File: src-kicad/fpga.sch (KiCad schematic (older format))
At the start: 4 parts, among them U1 iCE40HX1K-TQ144

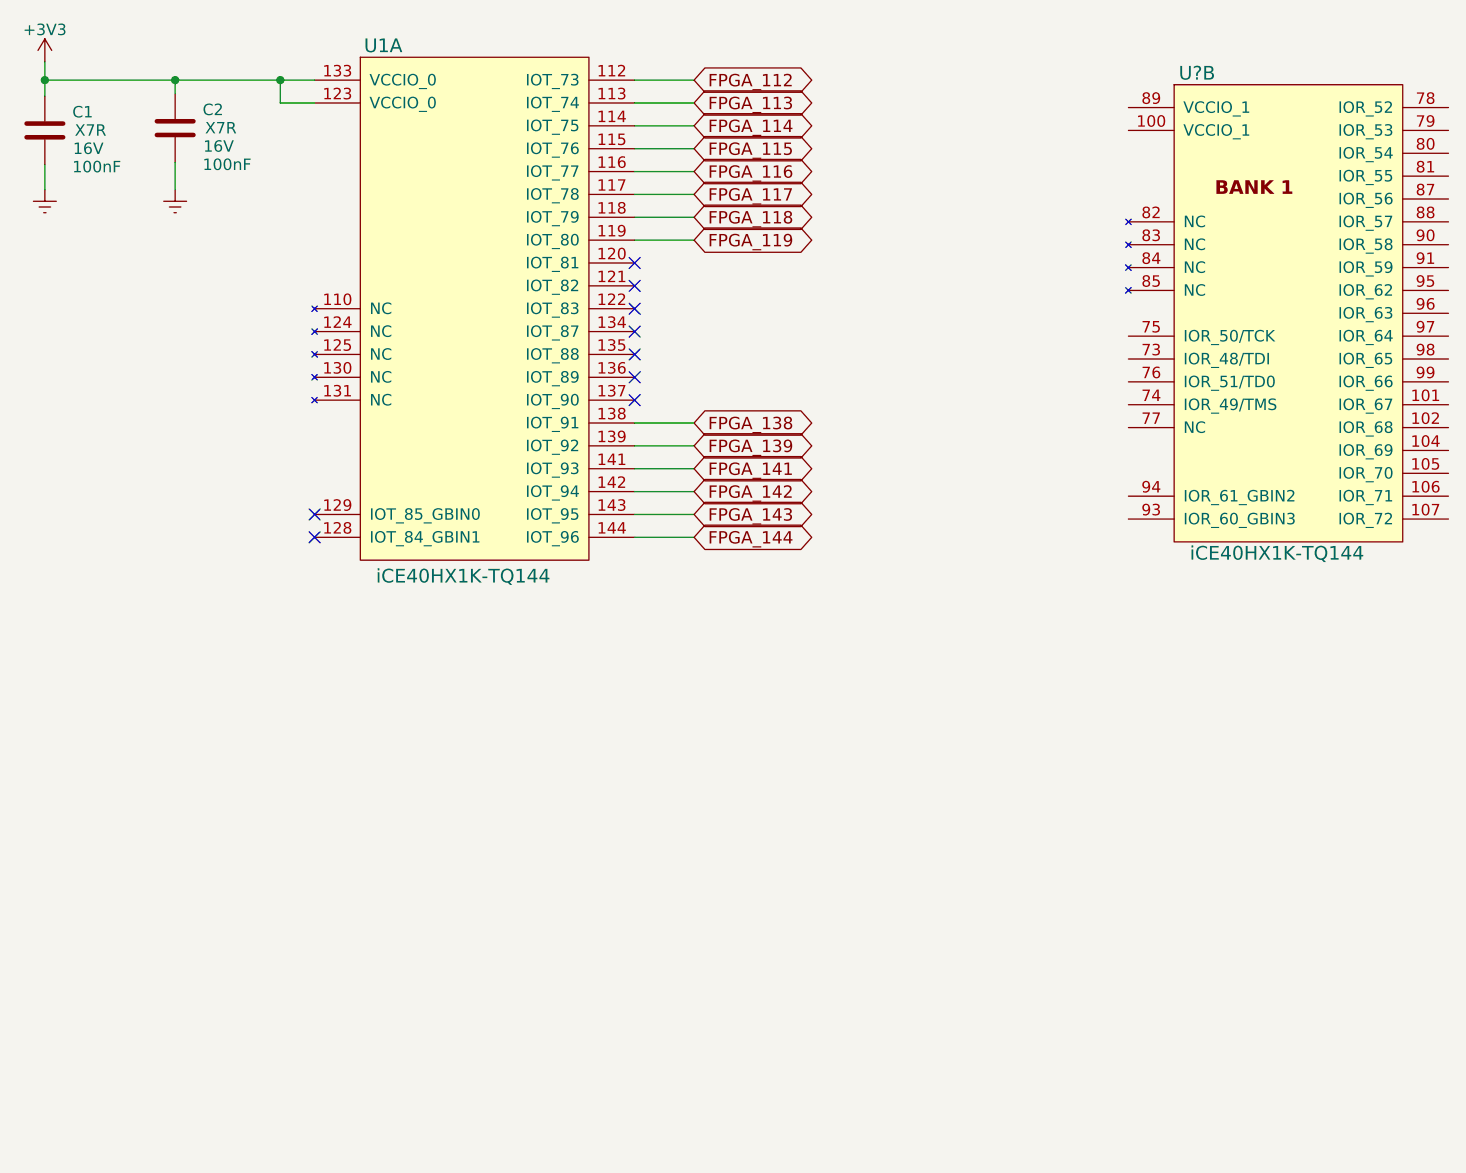
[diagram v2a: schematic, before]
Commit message: Kicad. FPGA: Bank 1 added to schematic
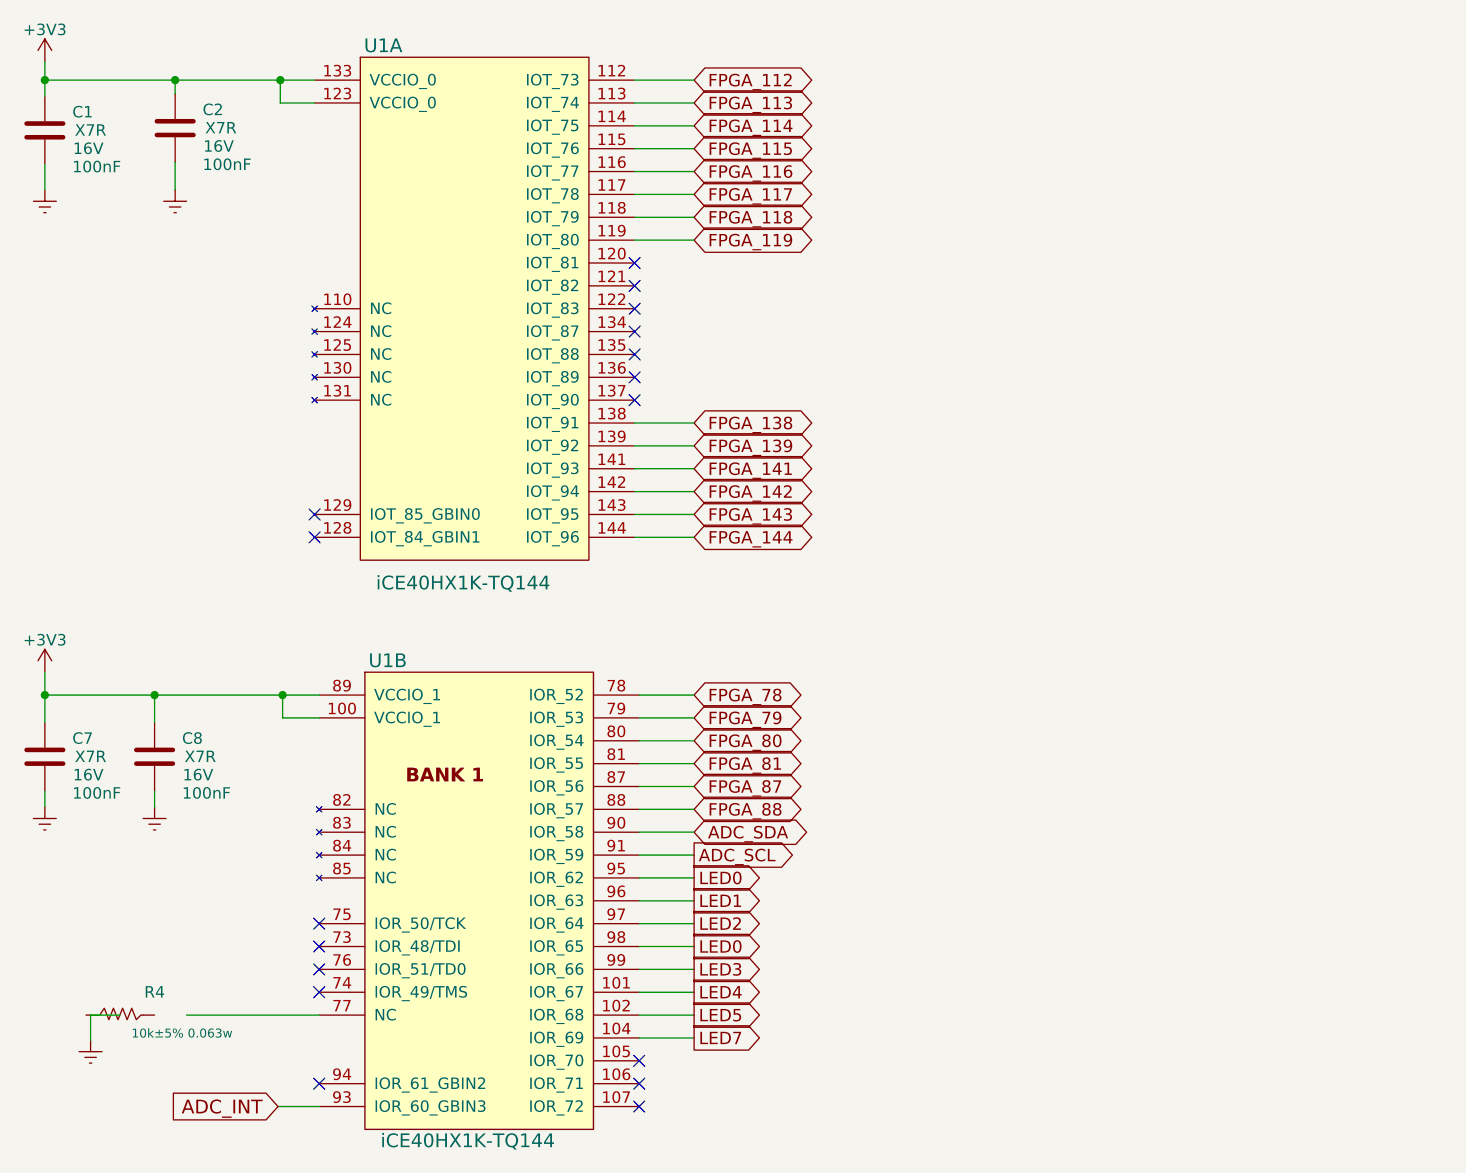
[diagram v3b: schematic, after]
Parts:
- added C7, C8: 100nF, symbol C
- added R4: 10k±5% 0.063w, symbol R
- gave numbers to parts that had none: 1
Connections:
- net labels added: ADC_INT, ADC_SCL, ADC_SDA, FPGA_78, FPGA_79, FPGA_80, FPGA_81, FPGA_87, FPGA_88, LED0, LED1, LED2, LED3, LED4, LED5, LED7
- wire segments 21 -> 48
- no-connect marks 9 -> 17
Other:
- moved on the sheet: U1B
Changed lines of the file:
@@
 EESchema Schematic File Version 2
-LIBS:power
-LIBS:device
 LIBS:transistors
 LIBS:conn
@@
 $EndDescr
 $Comp
-L iCE40HX1K-TQ144 U1
-U 1 1 5742DE36
-P 2140 1010
-F 0 "U1" H 2440 1160 60  0000 C CNN
-F 1 "iCE40HX1K-TQ144" H 2790 -1160 60  0000 C CNN
-F 2 "" H 2440 610 60  0000 C CNN
-F 3 "" H 2440 610 60  0000 C CNN
-	1    2140 1010
-	1    0    0    -1
-$EndComp
-$Comp
 L C C1
 U 1 1 5742E2A9
@@
 $EndComp
 $Comp
-L +3V3 #PWR?
+L +3V3 #PWR01
 U 1 1 5742EB21
 P 960 930
-F 0 "#PWR?" H 960 780 50  0001 C CNN
+F 0 "#PWR01" H 960 780 50  0001 C CNN
 F 1 "+3V3" H 960 1070 50  0000 C CNN
 F 2 "" H 960 930 50  0000 C CNN
@@
 	1    0    0    -1
 $EndComp
-Wire Wire Line
-	960  930  960  1080
-$Comp
-L GNDREF #PWR?
+$Comp
+L GNDREF #PWR02
 U 1 1 5742F120
 P 960 1490
-F 0 "#PWR?" H 960 1240 50  0001 C CNN
+F 0 "#PWR02" H 960 1240 50  0001 C CNN
 F 1 "GNDREF" H 960 1340 50  0001 C CNN
 F 2 "" H 960 1490 50  0000 C CNN
@@
 	1    0    0    -1
 $EndComp
-Wire Wire Line
-	960  1490 960  1380
 $Comp
 L C C2
@@
 $EndComp
 $Comp
-L GNDREF #PWR?
+L GNDREF #PWR03
 U 1 1 5742F317
 P 1530 1490
-F 0 "#PWR?" H 1530 1240 50  0001 C CNN
+F 0 "#PWR03" H 1530 1240 50  0001 C CNN
 F 1 "GNDREF" H 1530 1340 50  0001 C CNN
 F 2 "" H 1530 1490 50  0000 C CNN
@@
 	1    0    0    -1
 $EndComp
-Wire Wire Line
-	1530 1370 1530 1490
-Wire Wire Line
-	960  1010 2140 1010
-Connection ~ 960  1010
-Wire Wire Line
-	1530 1070 1530 1010
-Connection ~ 1530 1010
-Wire Wire Line
-	2140 1110 1990 1110
-Wire Wire Line
-	1990 1110 1990 1010
-Connection ~ 1990 1010
 NoConn ~ 2140 2910
 NoConn ~ 2140 3010
-Wire Wire Line
-	3540 1010 3800 1010
 Text GLabel 3800 1010 2    54   BiDi ~ 0
 FPGA_112
 Text GLabel 3800 1110 2    54   BiDi ~ 0
 FPGA_113
-Wire Wire Line
-	3540 1110 3800 1110
 Text GLabel 3800 1210 2    54   BiDi ~ 0
 FPGA_114
@@
 Text GLabel 3800 1710 2    54   BiDi ~ 0
 FPGA_119
-Wire Wire Line
-	3540 1210 3800 1210
-Wire Wire Line
-	3800 1310 3540 1310
-Wire Wire Line
-	3540 1410 3800 1410
-Wire Wire Line
-	3800 1510 3540 1510
-Wire Wire Line
-	3540 1610 3800 1610
-Wire Wire Line
-	3800 1710 3540 1710
 Text GLabel 3800 2510 2    54   BiDi ~ 0
 FPGA_138
@@
 Text GLabel 3800 3010 2    54   BiDi ~ 0
 FPGA_144
-Wire Wire Line
-	3540 3010 3800 3010
-Wire Wire Line
-	3800 2910 3540 2910
-Wire Wire Line
-	3540 2810 3800 2810
-Wire Wire Line
-	3800 2710 3540 2710
-Wire Wire Line
-	3540 2610 3800 2610
-Wire Wire Line
-	3540 2510 3800 2510
 NoConn ~ 3540 1810
 NoConn ~ 3540 1910
@@
 NoConn ~ 3540 2410
 $Comp
-L iCE40HX1K-TQ144 U?
+L iCE40HX1K-TQ144 U1
 U 2 1 57436BD0
-P 5700 1130
-F 0 "U?" H 6000 1280 60  0000 C CNN
-F 1 "iCE40HX1K-TQ144" H 6350 -820 60  0000 C CNN
-F 2 "" H 6000 730 60  0000 C CNN
-F 3 "" H 6000 730 60  0000 C CNN
-	2    5700 1130
-	1    0    0    -1
-$EndComp
+P 2160 3700
+F 0 "U1" H 2460 3850 60  0000 C CNN
+F 1 "iCE40HX1K-TQ144" H 2810 1750 60  0000 C CNN
+F 2 "" H 2460 3300 60  0000 C CNN
+F 3 "" H 2460 3300 60  0000 C CNN
+	2    2160 3700
+	1    0    0    -1
+$EndComp
+$Comp
+L C C7
+U 1 1 5743AB85
+P 960 3970
+F 0 "C7" H 1080 4050 50  0000 L CNN
+F 1 "100nF" H 1080 3810 50  0000 L CNN
+F 2 "" H 998 3820 50  0000 C CNN
+F 3 "" H 960 3970 50  0000 C CNN
+F 4 "X7R" H 1160 3970 50  0000 C CNN "class"
+F 5 "16V" H 1150 3890 50  0000 C CNN "Voltage"
+	1    960  3970
+	1    0    0    -1
+$EndComp
+$Comp
+L +3V3 #PWR04
+U 1 1 5743AD45
+P 960 3600
+F 0 "#PWR04" H 960 3450 50  0001 C CNN
+F 1 "+3V3" H 960 3740 50  0000 C CNN
+F 2 "" H 960 3600 50  0000 C CNN
+F 3 "" H 960 3600 50  0000 C CNN
+	1    960  3600
+	1    0    0    -1
+$EndComp
+$Comp
+L GNDREF #PWR05
+U 1 1 5743B1A8
+P 960 4190
+F 0 "#PWR05" H 960 3940 50  0001 C CNN
+F 1 "GNDREF" H 960 4040 50  0001 C CNN
+F 2 "" H 960 4190 50  0000 C CNN
+F 3 "" H 960 4190 50  0000 C CNN
+	1    960  4190
+	1    0    0    -1
+$EndComp
+$Comp
+L C C8
+U 1 1 5743B372
+P 1440 3970
+F 0 "C8" H 1560 4050 50  0000 L CNN
+F 1 "100nF" H 1560 3810 50  0000 L CNN
+F 2 "" H 1478 3820 50  0000 C CNN
+F 3 "" H 1440 3970 50  0000 C CNN
+F 4 "X7R" H 1640 3970 50  0000 C CNN "class"
+F 5 "16V" H 1630 3890 50  0000 C CNN "Voltage"
+	1    1440 3970
+	1    0    0    -1
+$EndComp
+$Comp
+L GNDREF #PWR06
+U 1 1 5743B3FC
+P 1440 4190
+F 0 "#PWR06" H 1440 3940 50  0001 C CNN
+F 1 "GNDREF" H 1440 4040 50  0001 C CNN
+F 2 "" H 1440 4190 50  0000 C CNN
+F 3 "" H 1440 4190 50  0000 C CNN
+	1    1440 4190
+	1    0    0    -1
+$EndComp
+$Comp
+L iCE40HX1K-TQ144 U1
+U 1 1 5743108E
+P 2140 1010
+F 0 "U1" H 2440 1160 60  0000 C CNN
+F 1 "iCE40HX1K-TQ144" H 2790 -1190 60  0000 C CNN
+F 2 "" H 2440 610 60  0000 C CNN
+F 3 "" H 2440 610 60  0000 C CNN
+	1    2140 1010
+	1    0    0    -1
+$EndComp
+$Comp
+L R R4
+U 1 1 574319A2
+P 1440 5100
+F 0 "R4" V 1340 5100 50  0000 C CNN
+F 1 "10k±5% 0.063w" V 1520 5220 39  0000 C CNN
+F 2 "" V 1370 5100 50  0000 C CNN
+F 3 "" H 1440 5100 50  0000 C CNN
+	1    1440 5100
+	0    1    1    0
+$EndComp
+$Comp
+L GNDREF #PWR07
+U 1 1 57431C0E
+P 1160 5210
+F 0 "#PWR07" H 1160 4960 50  0001 C CNN
+F 1 "GNDREF" H 1160 5060 50  0001 C CNN
+F 2 "" H 1160 5210 50  0000 C CNN
+F 3 "" H 1160 5210 50  0000 C CNN
+	1    1160 5210
+	1    0    0    -1
+$EndComp
+Wire Wire Line
+	960  930  960  1080
+Wire Wire Line
+	960  1490 960  1380
+Wire Wire Line
+	1530 1370 1530 1490
+Wire Wire Line
+	960  1010 2140 1010
+Connection ~ 960  1010
+Wire Wire Line
+	1530 1070 1530 1010
+Connection ~ 1530 1010
+Wire Wire Line
+	2140 1110 1990 1110
+Wire Wire Line
+	1990 1110 1990 1010
+Connection ~ 1990 1010
+Wire Wire Line
+	3540 1010 3800 1010
+Wire Wire Line
+	3540 1110 3800 1110
+Wire Wire Line
+	3540 1210 3800 1210
+Wire Wire Line
+	3800 1310 3540 1310
+Wire Wire Line
+	3540 1410 3800 1410
+Wire Wire Line
+	3800 1510 3540 1510
+Wire Wire Line
+	3540 1610 3800 1610
+Wire Wire Line
+	3800 1710 3540 1710
+Wire Wire Line
+	3540 3010 3800 3010
+Wire Wire Line
+	3800 2910 3540 2910
+Wire Wire Line
+	3540 2810 3800 2810
+Wire Wire Line
+	3800 2710 3540 2710
+Wire Wire Line
+	3540 2610 3800 2610
+Wire Wire Line
+	3540 2510 3800 2510
+Wire Wire Line
+	960  3600 960  3820
+Wire Wire Line
+	960  3700 2160 3700
+Connection ~ 960  3700
+Wire Wire Line
+	2160 3800 2000 3800
+Wire Wire Line
+	2000 3800 2000 3700
+Connection ~ 2000 3700
+Wire Wire Line
+	960  4190 960  4120
+Wire Wire Line
+	1440 4190 1440 4120
+Wire Wire Line
+	1440 3820 1440 3700
+Connection ~ 1440 3700
+Wire Wire Line
+	1580 5100 2160 5100
+Wire Wire Line
+	1290 5100 1160 5100
+Wire Wire Line
+	1160 5100 1160 5210
+NoConn ~ 2160 4700
+NoConn ~ 2160 4800
+NoConn ~ 2160 4900
+NoConn ~ 2160 5000
+NoConn ~ 2160 5400
+Text GLabel 1980 5500 0    60   Input ~ 0
+ADC_INT
+Wire Wire Line
+	2160 5500 1980 5500
+Text GLabel 3800 3700 2    54   BiDi ~ 0
+FPGA_78
+Text GLabel 3800 3800 2    54   BiDi ~ 0
+FPGA_79
+Text GLabel 3800 3900 2    54   BiDi ~ 0
+FPGA_80
+Text GLabel 3800 4000 2    54   BiDi ~ 0
+FPGA_81
+Text GLabel 3800 4100 2    54   BiDi ~ 0
+FPGA_87
+Text GLabel 3800 4200 2    54   BiDi ~ 0
+FPGA_88
+Wire Wire Line
+	3800 3700 3560 3700
+Wire Wire Line
+	3800 3800 3560 3800
+Wire Wire Line
+	3800 3900 3560 3900
+Wire Wire Line
+	3800 4000 3560 4000
+Wire Wire Line
+	3800 4100 3560 4100
+Wire Wire Line
+	3800 4200 3560 4200
+Text GLabel 3800 4300 2    54   BiDi ~ 0
+ADC_SDA
+Text GLabel 3800 4400 2    54   Output ~ 0
+ADC_SCL
+Wire Wire Line
+	3800 4300 3560 4300
+Wire Wire Line
+	3800 4400 3560 4400
+NoConn ~ 3560 5500
+NoConn ~ 3560 5400
+NoConn ~ 3560 5300
+Text GLabel 3800 4500 2    54   Output ~ 0
+LED0
+Text GLabel 3800 4600 2    54   Output ~ 0
+LED1
+Text GLabel 3800 4700 2    54   Output ~ 0
+LED2
+Text GLabel 3800 4800 2    54   Output ~ 0
+LED0
+Text GLabel 3800 4900 2    54   Output ~ 0
+LED3
+Text GLabel 3800 5000 2    54   Output ~ 0
+LED4
+Text GLabel 3800 5100 2    54   Output ~ 0
+LED5
+Text GLabel 3800 5200 2    54   Output ~ 0
+LED7
+Wire Wire Line
+	3800 4500 3560 4500
+Wire Wire Line
+	3560 4600 3800 4600
+Wire Wire Line
+	3560 4700 3800 4700
+Wire Wire Line
+	3800 4800 3560 4800
+Wire Wire Line
+	3560 4900 3800 4900
+Wire Wire Line
+	3800 5000 3560 5000
+Wire Wire Line
+	3560 5100 3800 5100
+Wire Wire Line
+	3800 5200 3560 5200
 $EndSCHEMATC

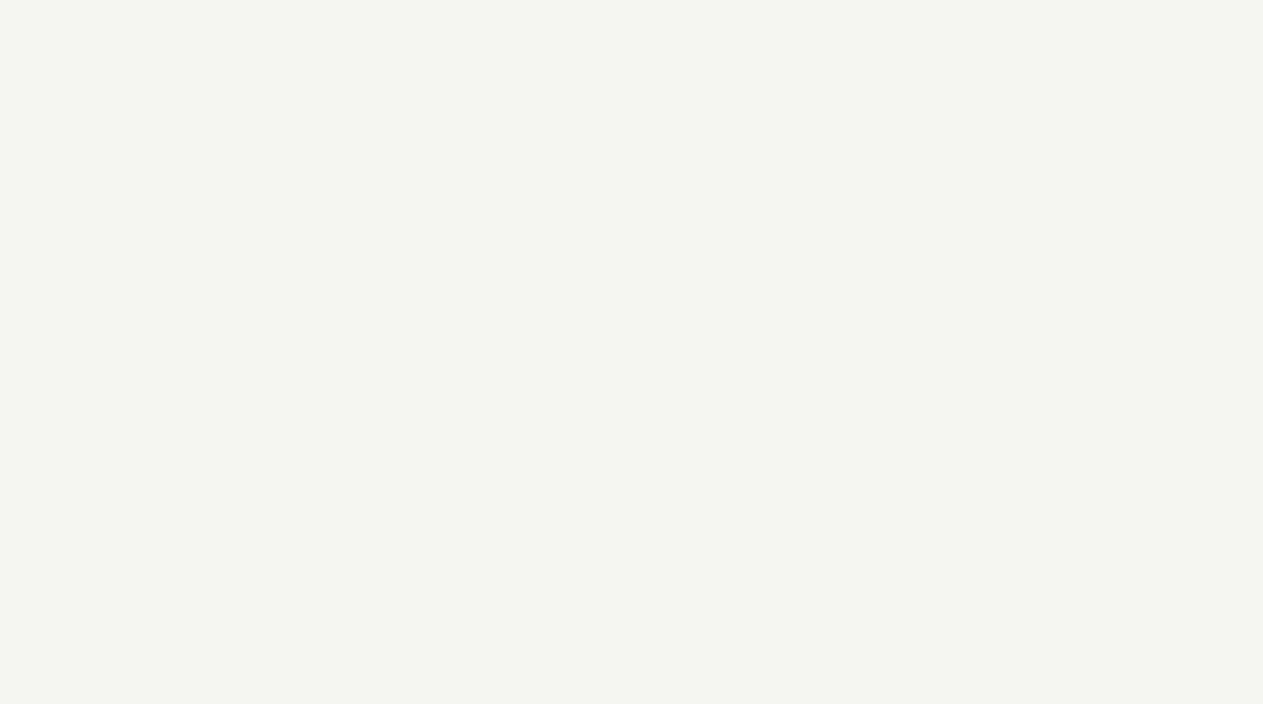
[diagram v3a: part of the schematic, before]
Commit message: Kicad. FPGA. Bank3 connected
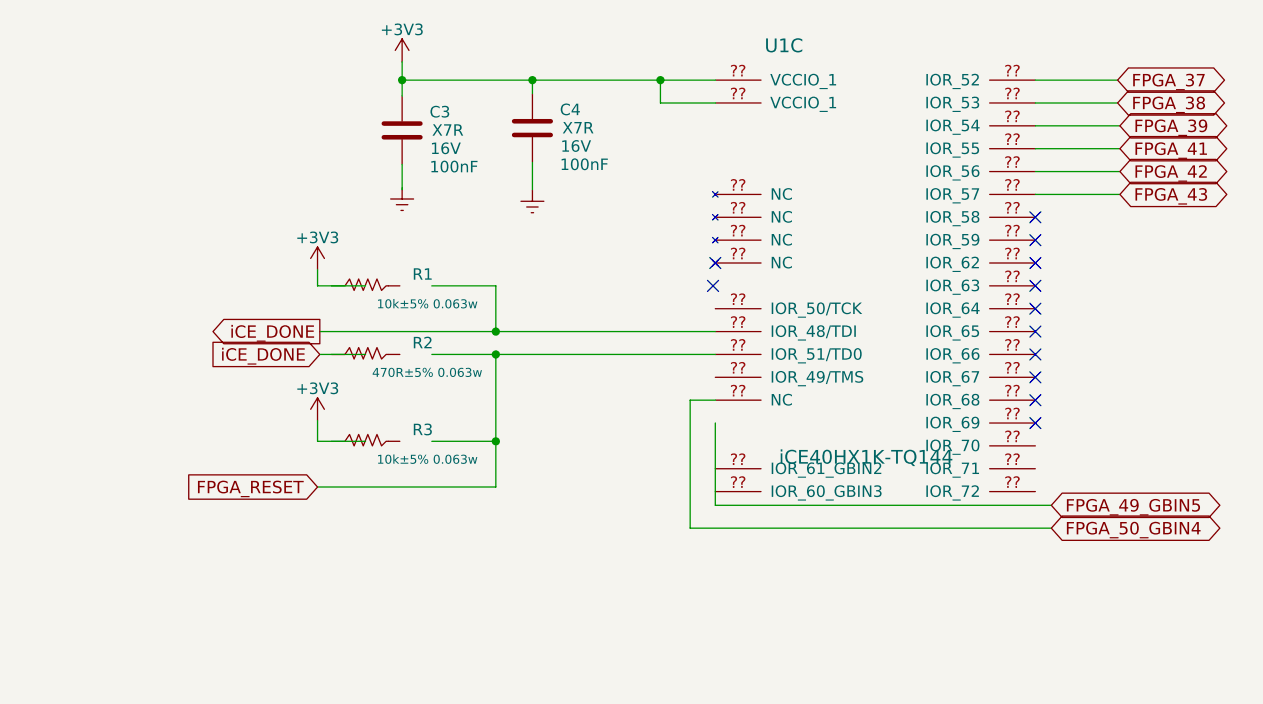
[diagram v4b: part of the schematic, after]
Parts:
- added C3, C4: 100nF, symbol C
- added R1, R3: 10k±5% 0.063w, symbol R
- added R2: 470R±5% 0.063w, symbol R
- added unit 3 of U1
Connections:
- net labels added: FPGA_37, FPGA_38, FPGA_39, FPGA_41, FPGA_42, FPGA_43, FPGA_49_GBIN5, FPGA_50_GBIN4, FPGA_RESET, iCE_DONE
- wire segments 48 -> 78
- no-connect marks 17 -> 29
